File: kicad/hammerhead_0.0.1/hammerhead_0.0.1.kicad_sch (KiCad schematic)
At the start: 28 parts, among them J1 BATTERY_CONN, J2 M1_CONN, J3 M2_CONN, J4 JTAG, J5 DEBUG, J6 MM_DB_CONN, U1 STM32F103C8T6, U2 25LC256-I_SN, Y1 16 MHz

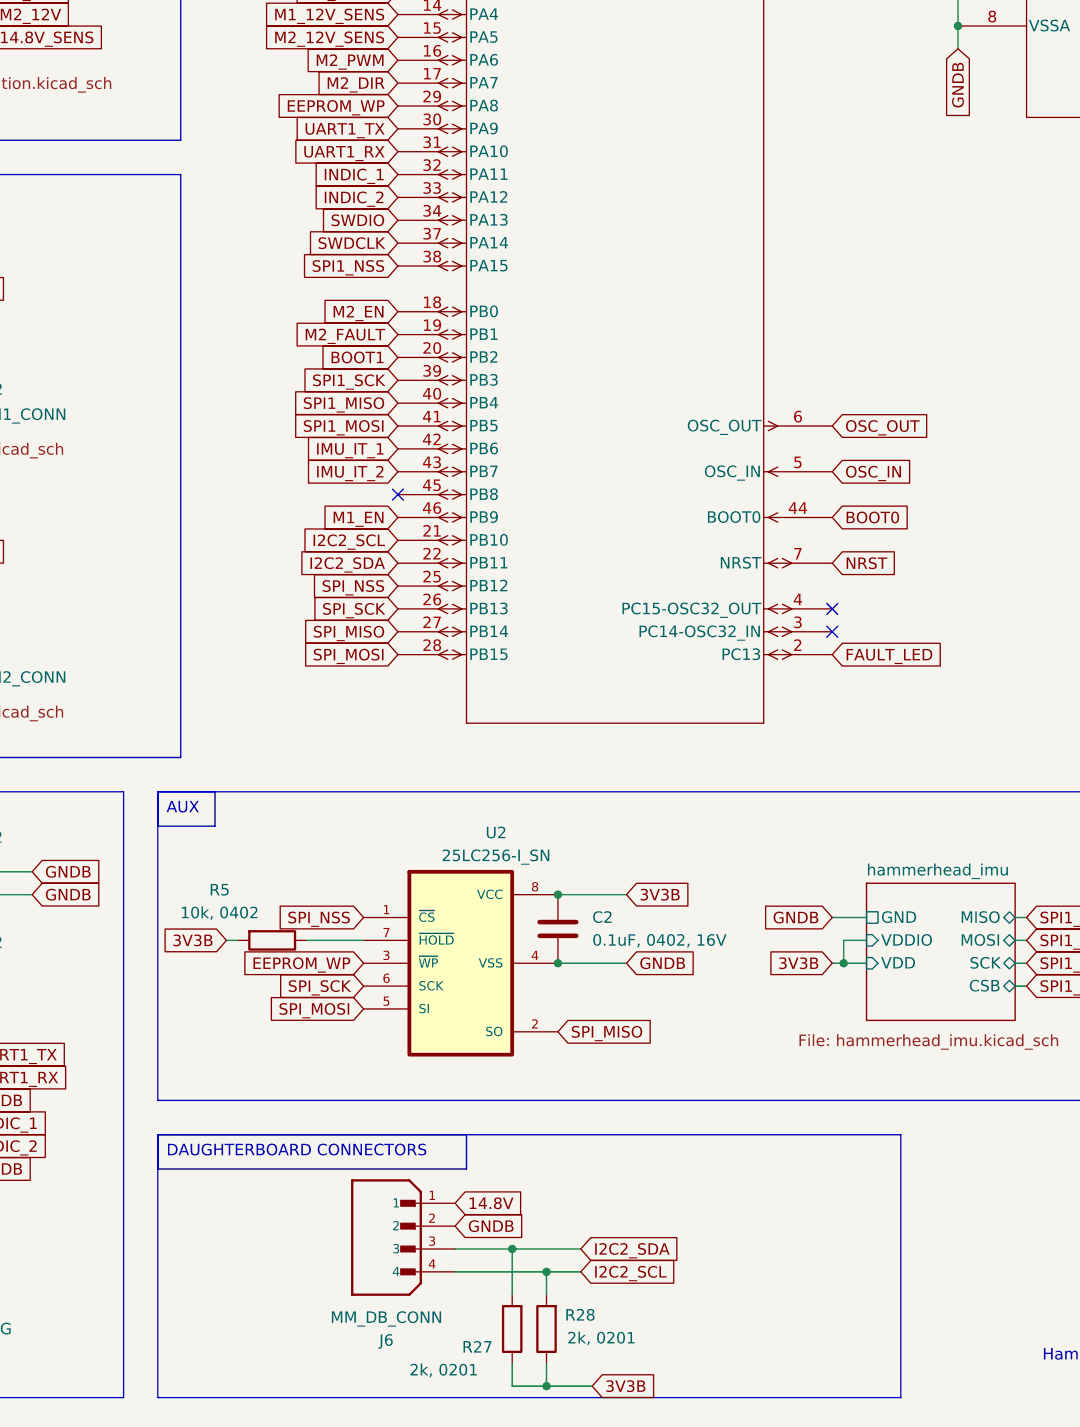
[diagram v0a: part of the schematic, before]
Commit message: replace i2c comms with can
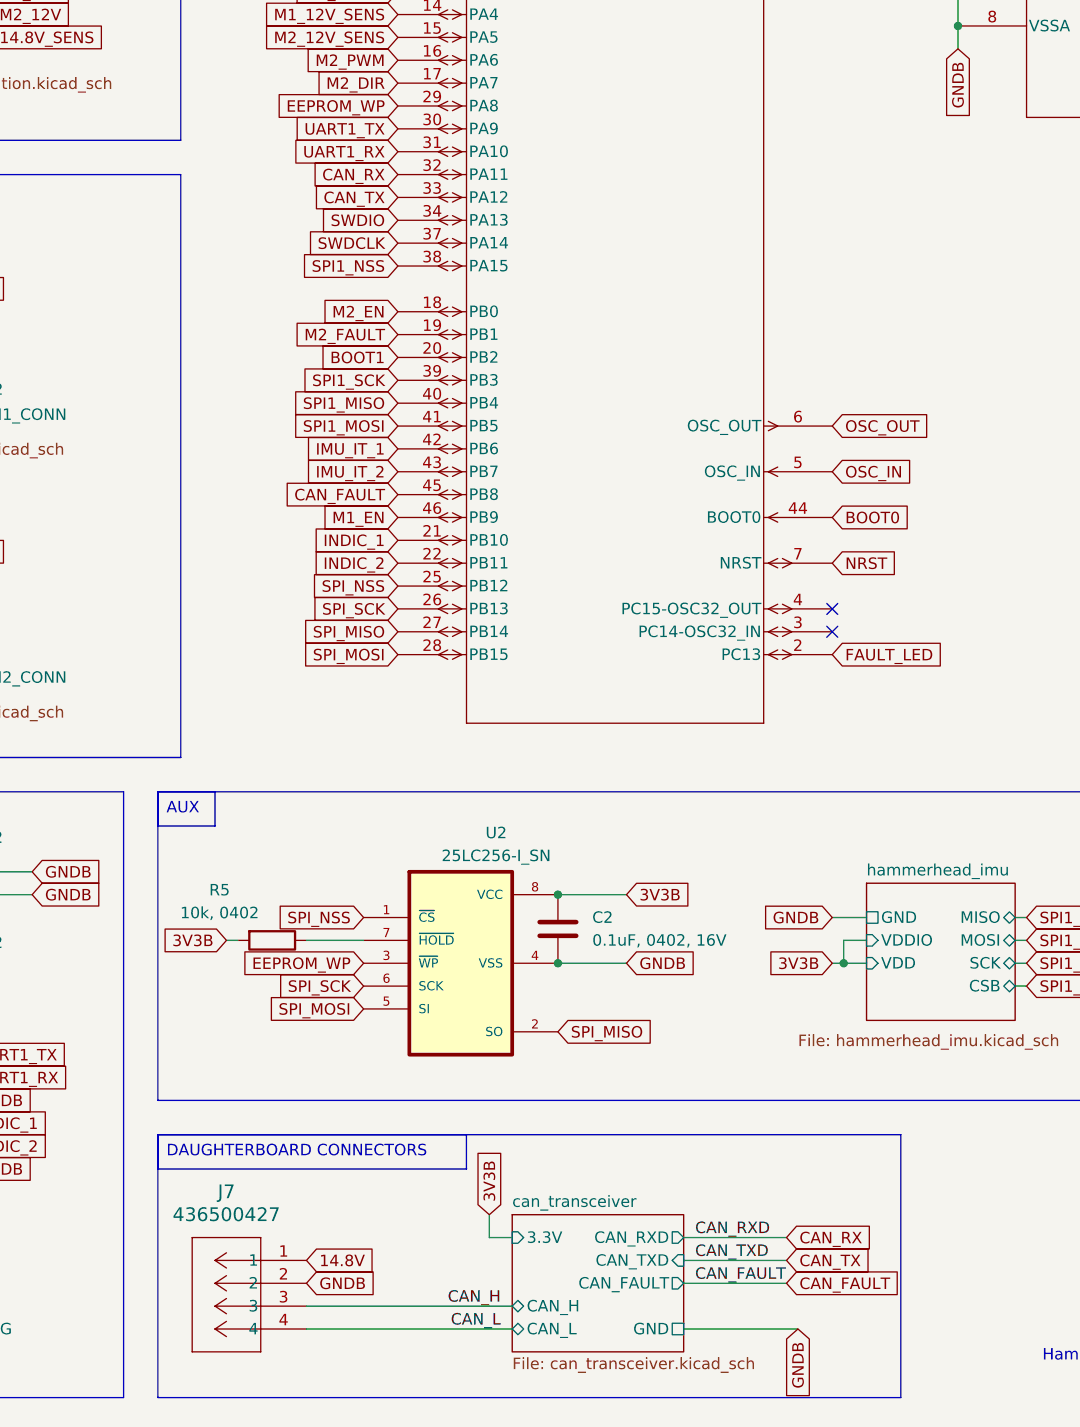
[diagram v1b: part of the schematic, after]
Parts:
- removed J6: MM_DB_CONN, B4B_XH_A:JST_B4B-XH-A, symbol B4B_XH_A:B4B-XH-A
- removed R27, R28: 2k, 0201, Resistor_SMD:R_0201_0603Metric, symbol Device:R
- added J7: 436500427, CONN_SD-43650-010_04_MOL, symbol 436500427:436500427
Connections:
- net I2C2_SCL is gone; now on net INDIC_1: U1.21 (PB10)
- net I2C2_SDA is gone; now on net INDIC_2: U1.22 (PB11)
- net 14.8V: now also J7.1
- net GNDB: now also J7.2
- net INDIC_1: no longer U1.32 (PA11)
- net INDIC_2: no longer U1.33 (PA12)
- net CAN_FAULT: now reaches U1.45 (PB8)
- new net CAN_H: J7.3
- new net CAN_L: J7.4
- new net CAN_RX: U1.32 (PA11)
- new net CAN_TX: U1.33 (PA12)
- no-connect marks 6 -> 5
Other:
- added sheet can_transceiver (can_transceiver.kicad_sch)

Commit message: move thirdparty models to thirdparty dir
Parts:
- J7: footprint CONN_SD-43650-010_04_MOL -> 436500427:CONN_SD-43650-010_04_MOL
- U2: footprint 25LC256-I/SN:SOIC127P599X175-8N -> 25LC256-I/SN:SOIC8-N_MC_MCH
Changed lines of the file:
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@@
 			)
 		)
-		(property "Footprint" "CONN_SD-43650-010_04_MOL"
+		(property "Footprint" "436500427:CONN_SD-43650-010_04_MOL"
 			(at 106.68 186.69 0)
 			(effects
@@
 			)
 		)
-		(property "Footprint" "25LC256-I/SN:SOIC127P599X175-8N"
+		(property "Footprint" "25LC256-I/SN:SOIC8-N_MC_MCH"
 			(at 130.81 151.13 0)
 			(effects
